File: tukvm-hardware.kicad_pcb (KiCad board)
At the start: 2 copper layers, 90.5 x 68.9 mm, 97 parts, among them J1 PCIexpress_x1, J2 PCIexpress_bracket, J3 HDMI_A, J4 USB_C_Receptacle_USB2.0, J5 Conn_02x08_Odd_Even, J6 USB_9P, J7 Conn_01x04, U1 M24C64-RMN6TP, U10 TLP172GM, U11 CH340N, U2 MS2109, U3 MCORE-H616, U4 DP1435-5V, U5 TLP172GM, U6 TLP172GM, U7 MT3520B, U8 MT3520B, U9 TLP172GM, Y1 24MHz 12pF

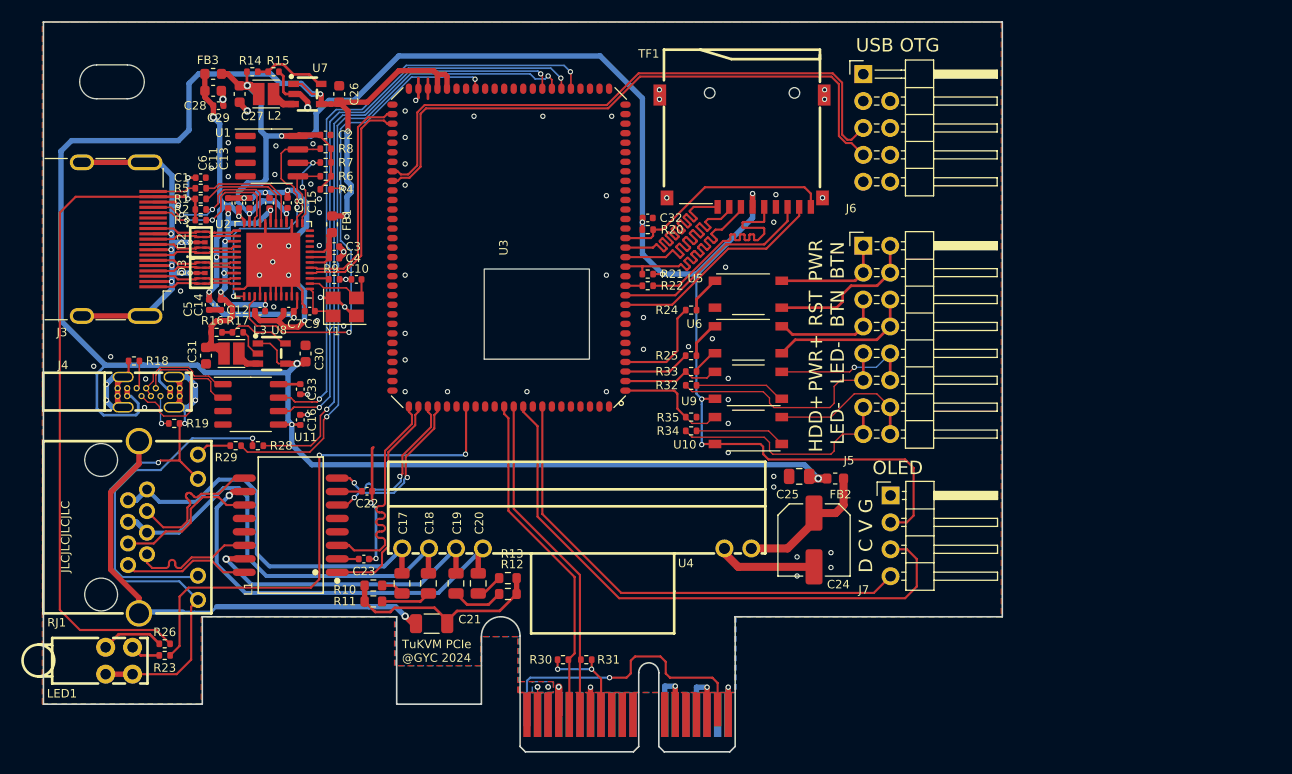
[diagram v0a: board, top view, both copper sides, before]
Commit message: Update pcb & sch for T113 SOM
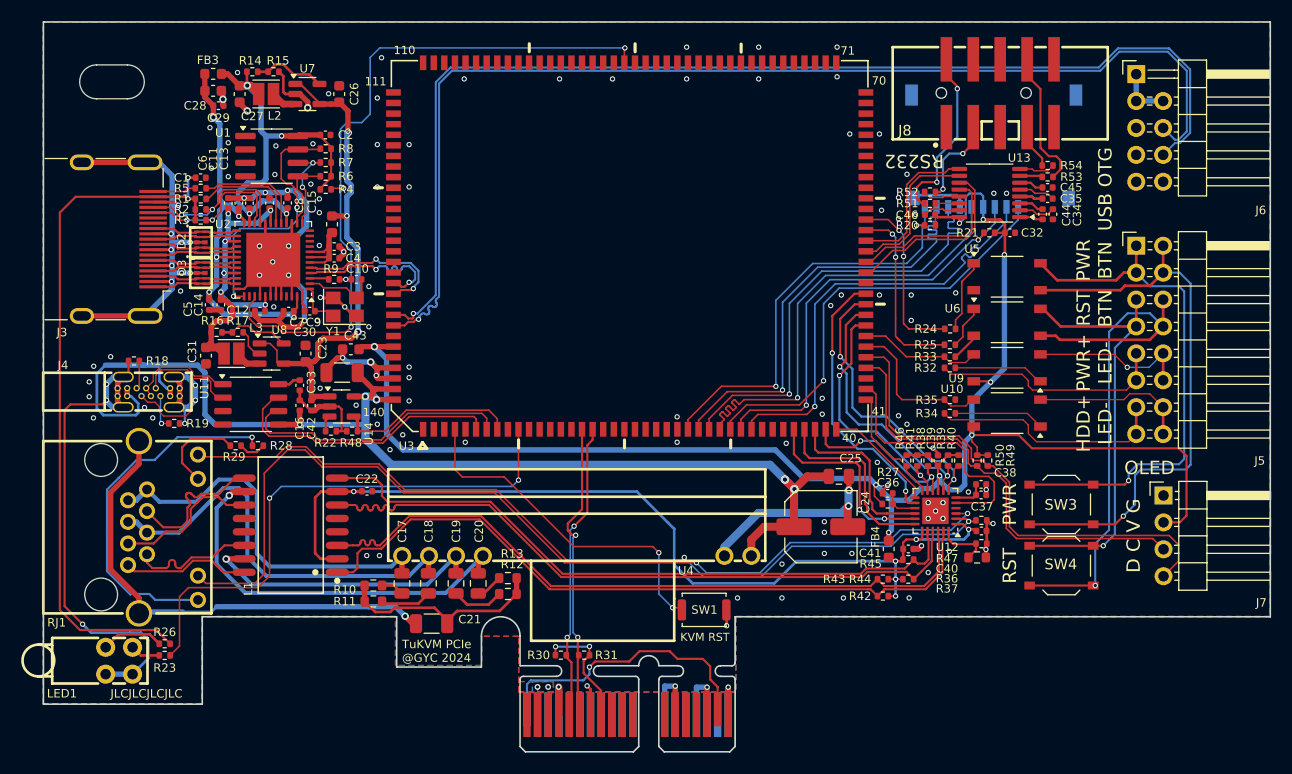
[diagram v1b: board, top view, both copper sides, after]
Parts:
- removed FB2: 600Ω@100MHz, Inductor_SMD:L_0603_1608Metric
- added C34: 100nF, Capacitor_SMD:C_0402_1005Metric, F.Cu at (158.8, 143.4)
- added C35: 100nF, Capacitor_SMD:C_0402_1005Metric, F.Cu at (159.3, 141.9)
- added C36: 100nF, Capacitor_SMD:C_0402_1005Metric, F.Cu at (144.2, 169.7)
- added C37: 100nF, Capacitor_SMD:C_0402_1005Metric, F.Cu at (153.0, 169.9)
- added C38: 1uF, Capacitor_SMD:C_0402_1005Metric, F.Cu at (153.0, 168.9)
- added C39: 100nF, Capacitor_SMD:C_0402_1005Metric, F.Cu at (148.9, 166.6)
- added C40: 100nF, Capacitor_SMD:C_0402_1005Metric, F.Cu at (153.0, 173.3)
- added C41: 100nF, Capacitor_SMD:C_0402_1005Metric, F.Cu at (146.1, 175.0)
- added C42: 1uF, Capacitor_SMD:C_0402_1005Metric, F.Cu at (89.8, 161.4)
- added C43: 10uF, Capacitor_SMD:C_0603_1608Metric, F.Cu at (93.5, 156.1)
- added C44: 100nF, Capacitor_SMD:C_0402_1005Metric, F.Cu at (159.8, 143.4)
- added C45: 100nF, Capacitor_SMD:C_0402_1005Metric, F.Cu at (159.3, 140.8)
- added C46: 100nF, Capacitor_SMD:C_0402_1005Metric, F.Cu at (148.2, 143.4)
- added FB4: 600Ω@100MHz, Inductor_SMD:L_0603_1608Metric, F.Cu at (144.3, 175.0)
- added J8: RS232_MALE, easyeda2kicad:IDC-SMD_10P-P2.54-V-R2-C5-S9.50, F.Cu at (154.8, 131.9)
- added R27: 5.1kΩ, Resistor_SMD:R_0402_1005Metric, F.Cu at (144.2, 170.7)
- added R36: 22kΩ, Resistor_SMD:R_0402_1005Metric, F.Cu at (153.0, 174.5)
- added R37: 27kΩ, Resistor_SMD:R_0603_1608Metric, F.Cu at (152.6, 175.8)
- added R38: 5.1kΩ, Resistor_SMD:R_0402_1005Metric, F.Cu at (148.0, 166.6)
- added R39: 5.1kΩ, Resistor_SMD:R_0402_1005Metric, F.Cu at (149.9, 166.6)
- added R40: 5.1kΩ, Resistor_SMD:R_0402_1005Metric, F.Cu at (150.9, 166.6)
- added R41: 5.1kΩ, Resistor_SMD:R_0402_1005Metric, F.Cu at (147.0, 166.6)
- added R42: 49.9Ω, Resistor_SMD:R_0402_1005Metric, F.Cu at (143.7, 179.4)
- added R43: 49.9Ω, Resistor_SMD:R_0402_1005Metric, F.Cu at (143.7, 177.8)
- added R44: 49.9Ω, Resistor_SMD:R_0402_1005Metric, F.Cu at (146.1, 177.8)
- added R45: 49.9Ω, Resistor_SMD:R_0402_1005Metric, F.Cu at (146.1, 176.0)
- added R46: 1.5kΩ, Resistor_SMD:R_0402_1005Metric, F.Cu at (146.0, 166.6)
- added R47: 10kΩ, Resistor_SMD:R_0402_1005Metric, F.Cu at (153.0, 172.3)
- added R48: 5.1kΩ, Resistor_SMD:R_0402_1005Metric, F.Cu at (93.6, 163.9)
- added R49: 5.1kΩ, Resistor_SMD:R_0402_1005Metric, F.Cu at (153.6, 166.6)
- added R50: 5.1kΩ, Resistor_SMD:R_0402_1005Metric, F.Cu at (152.6, 166.6)
- added R51: 0Ω, Resistor_SMD:R_0402_1005Metric, F.Cu at (148.2, 142.3)
- added R52: 0Ω, Resistor_SMD:R_0402_1005Metric, F.Cu at (148.2, 141.3)
- added R53: 0Ω, Resistor_SMD:R_0402_1005Metric, F.Cu at (159.3, 139.8)
- added R54: 0Ω, Resistor_SMD:R_0402_1005Metric, F.Cu at (159.3, 138.8)
- added SW1: SKRK, Button_Switch_SMD:SW_Push_SPST_NO_Alps_SKRK, F.Cu at (126.8, 180.7)
- added SW3: TS-1187A, Button_Switch_SMD:SW_Push_1P1T_XKB_TS-1187A, F.Cu at (160.6, 170.8)
- added SW4: TS-1187A, Button_Switch_SMD:SW_Push_1P1T_XKB_TS-1187A, F.Cu at (160.6, 176.6)
- added U12: LAN8720A, Package_DFN_QFN:VQFN-24-1EP_4x4mm_P0.5mm_EP2.5x2.5mm, F.Cu at (148.7, 171.4)
- added U13: SP3232EEY, Package_SO:TSSOP-16_4.4x5mm_P0.65mm, F.Cu at (153.8, 141.4)
- added U14: SY6280AAC, Package_TO_SOT_SMD:SOT-23-5, F.Cu at (92.6, 161.5)
- C22: value 100nF -> 22pF
- C23: value 100nF -> 100uF 6.3V; footprint Capacitor_SMD:C_0402_1005Metric -> Capacitor_SMD:C_1206_3216Metric
- R14: value 680kΩ -> 100kΩ
- R15, R16, R17: value 150kΩ -> 22kΩ
- R22: value 33Ω -> 22kΩ
- TF1: moved to B.Cu
- U3: value MCORE-H616 -> TLT113-SOM; footprint tukvm:MCORE-H616 -> tukvm:SMD_140P_35X45_SOM_TLT113_PackageLength
- U7, U8: footprint easyeda2kicad:SOT-23-5_L3.0-W1.7-P0.95-LS2.8-BR -> Package_TO_SOT_SMD:SOT-23-5
- moved C32 34.2 mm to (155.7, 145.1)
- moved R22 32.9 mm to (91.6, 163.9), turned to 0 degrees
- moved R21 32.5 mm to (153.8, 145.1)
- moved R20 26.7 mm to (148.2, 144.4), turned to 0 degrees
- moved J7 25.8 mm to (170.2, 169.9)
- moved J5 25.8 mm to (167.6, 146.3)
- moved J6 25.8 mm to (167.6, 135.2)
- moved R24 24.5 mm to (150.1, 154.2)
- moved R32 24.5 mm to (150.1, 157.9)
- moved R34 24.5 mm to (150.1, 162.2)
- moved R35 24.5 mm to (150.1, 160.9)
- moved U10 24.5 mm to (155.5, 162.1)
- moved U5 24.5 mm to (155.5, 149.3)
- moved U6 24.5 mm to (155.5, 153.6)
- moved U9 24.5 mm to (155.5, 157.9)
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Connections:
- net +1V2 renamed MS_1V2
- net +3.3VA renamed MS_3V3A
- C13 pad 2: +3.3V -> MS_3V3
- C15 pad 2: +3.3V -> MS_3V3
- C2 pad 2: +3.3V -> MS_3V3
- C22 pad 1: Earth -> PHY_VDDA
- C22 pad 2: Net-(L1-RCT) -> Earth
- C23 pad 1: Earth -> +5V
- C23 pad 2: Net-(L1-TCT) -> Earth
- C24 pad 1: Net-(U4-+5V) -> +5V
- C26 pad 2: +5V -> MS_5V
- C27 pad 2: +3.3V -> MS_3V3
- C30 pad 2: +5V -> MS_5V
- FB1 pad 2: +5V -> MS_5V
- FB3 pad 1: +3.3V -> MS_3V3
- J6 pad 5: /OTG_D- -> unconnected-(J6-Pin_5-Pad5)
- J6 pad 6: unconnected-(J6-Pin_6-Pad6) -> /OTG_D-
- J6 pad 7: /OTG_D+ -> unconnected-(J6-Pin_7-Pad7)
- J6 pad 8: unconnected-(J6-Pin_8-Pad8) -> /OTG_D+
- L1 pad 1: /PHY_RD+ -> /ETH PoE/PHY_RD+
- L1 pad 2: Net-(L1-TCT) -> PHY_VDDA
- L1 pad 3: /PHY_RD- -> /ETH PoE/PHY_RD-
- L1 pad 6: /PHY_TD+ -> /ETH PoE/PHY_TD+
- L1 pad 7: Net-(L1-RCT) -> PHY_VDDA
- L1 pad 8: /PHY_TD- -> /ETH PoE/PHY_TD-
- L2 pad 2: +3.3V -> MS_3V3
- R14 pad 1: +3.3V -> MS_3V3
- R22 pad 1: /TF_CLK -> Net-(U14-ISET)
- R22 pad 2: Net-(U3-PF2/SDC0_CLK/UART0_TX/PF_EINT2) -> Earth
- R28 pad 1: Net-(RJ1-R+) -> Net-(RJ1-R-)
- R28 pad 2: /PHY_ACT -> Earth
- R29 pad 1: Net-(RJ1-L+) -> Net-(RJ1-L-)
- R29 pad 2: /PHY_SPD -> Earth
- R4 pad 2: +3.3V -> MS_3V3
- R6 pad 1: +3.3V -> MS_3V3
- R7 pad 1: +3.3V -> MS_3V3
- R8 pad 1: +3.3V -> MS_3V3
- RJ1 pad 10: Earth -> Net-(RJ1-L-)
- RJ1 pad 11: Net-(RJ1-R+) -> /ETH PoE/LED1
- RJ1 pad 12: Earth -> Net-(RJ1-R-)
- RJ1 pad 9: Net-(RJ1-L+) -> /ETH PoE/LED2
- U1 pad 8: +3.3V -> MS_3V3
- U2 pad 16: +3.3V -> MS_3V3
- U2 pad 23: +3.3V -> MS_3V3
- U3 pad 1: /HDD_LED -> unconnected-(U3A-REFCLK_OUT-Pad1)
- U3 pad 10: /TF_D1 -> /HEART_BEAT_LED
- U3 pad 11: /TF_D0 -> unconnected-(U3A-PG2/SDC1_D0/UART3_RTS/RGMII_RXD1/RMII_RXD1/UART4_TX/PG_EINT2-Pad11)
- U3 pad 12: Net-(U3-PF2/SDC0_CLK/UART0_TX/PF_EINT2) -> unconnected-(U3A-PG1/SDC1_CMD/UART3_RX/RGMII_RXD0/RMII_RXD0/PWM6/PG_EINT1-Pad12)
- U3 pad 13: Earth -> unconnected-(U3A-PG0/SDC1_CLK/UART3_TX/RGMII_RXCTRL/RMII_CRS_DV/PWM7/PG_EINT0-Pad13)
- U3 pad 14: /TF_CMD -> unconnected-(U3A-PG10/PWM3/TWI3_SCK/RGMII_RXCK/CLK_FANOUT0/IR_RX/PG_EINT10-Pad14)
- U3 pad 15: /TF_D3 -> unconnected-(U3A-PG12/I2S1_LRCK/TWI0_SCK/RGMII_TXCTRL/RMII_TXEN/CLK_FANOUT2/PWM0/UART1_TX/PG_EINT12-Pad15)
- U3 pad 16: /TF_D2 -> /SMDAT
- U3 pad 17: /TF_DET -> /SMCLK
- U3 pad 2: /PWR_LED -> unconnected-(U3A-FEL-Pad2)
- U3 pad 25: unconnected-(U3-PI7/RGMII_TXD3/RMII_NULL/UART2_RTS/TS0_SYNC/TWI1_SCK/PI_EINT7-Pad25) -> Earth
- U3 pad 26: unconnected-(U3-PI8/RGMII_TXD2/RMII_NULL/UART2_CTS/TS0_DVLD/TWI1_SDA/PI_EINT8-Pad26) -> /TF_DET
- U3 pad 27: unconnected-(U3-PI9/RGMII_TXD1/RMII_TXD1/UART3_TX/TS0_D0/TWI2_SCK/PI_EINT9-Pad27) -> /TF_D1
- U3 pad 28: unconnected-(U3-PI10/RGMII_TXD0/RMII_TXD0/UART3_RX/TS0_D1/TWI2_SDA/PI_EINT10-Pad28) -> /TF_D0
- U3 pad 29: unconnected-(U3-PI11/RGMII_TXCK/RMII_TXCK/UART3_RTS/TS0_D2/PWM1/PI_EINT11-Pad29) -> /TF_CLK
- U3 pad 3: /ATX_RST -> unconnected-(U3A-NMI-Pad3)
- U3 pad 30: unconnected-(U3-PI12/RGMII_TXCTL/RMII_TXEN/UART3_CTS/TS0_D3/PWM2/PI_EINT12-Pad30) -> /TF_D2
- U3 pad 31: Earth -> /TF_CMD
- U3 pad 32: unconnected-(U3-PI13/RGMII_CLKIN/RMII_NULL/UART4_TX/TS0_D4/PWM3/PI_EINT13-Pad32) -> /TF_D3
- U3 pad 33: unconnected-(U3-PI14/MDC/UART4_RX/TS0_D5/PWM4/PI_EINT14-Pad33) -> Earth
- U3 pad 36: /U0TXD -> /RMII_TXD0
- U3 pad 37: /U0RXD -> /RMII_TXD1
- U3 pad 38: /PHY_SPD -> /RMII_TXEN
- U3 pad 39: /PHY_ACT -> /RMII_RXER
- U3 pad 4: /ATX_PWR -> Net-(U3A-RESET)
- U3 pad 40: unconnected-(U3-PH4/SPDIF_OUT/TWI3_SCK/PH_EINT4-Pad40) -> /RMII_MDC
- U3 pad 41: unconnected-(U3-PH5/UART2_TX/H_I2S3_MCLK/SPI1_CS0/TWI3_SDA/PH_EINT5-Pad41) -> /RMII_MDIO
- U3 pad 42: unconnected-(U3-PH6/UART2_RX/H_I2S3_BCLK/SPI1_CLK/TWI4_SCK/PH_EINT6-Pad42) -> /RMII_CLK25M
- U3 pad 44: unconnected-(U3-PH8/UART2_CTS/H_I2S3_DOUT0/SPI1_MISO/H_I2S3_DIN1/PH_EINT8-Pad44) -> /OLED_SCL
- U3 pad 45: unconnected-(U3-PH9/H_I2S3_DIN0/SPI1_CS1/H_I2S3_DOUT1/PH_EINT9-Pad45) -> /OLED_SDA
- U3 pad 46: /MS_STATUS -> /HDD_LED
- U3 pad 47: unconnected-(U3-PWRON-Pad47) -> /PWR_LED
- U3 pad 48: unconnected-(U3-VCC3V3-Pad48) -> /RMII_CRS_DV
- U3 pad 49: +5V -> /RMII_RXD0
- U3 pad 5: unconnected-(U3-PG10/H_I2S2_MCLK/X32KFOUT/AC_MCLK/PG_EINT10-Pad5) -> Earth
- U3 pad 50: +5V -> /RMII_RXD1
- U3 pad 51: Earth -> /RMII_REFCLK
- U3 pad 53: unconnected-(U3-RESET-Pad53) -> /M232_RXD
- U3 pad 54: Earth -> /M232_TXD
- U3 pad 55: /MS_USBD- -> /M232_CTS
- U3 pad 56: /MS_USBD+ -> /M232_RTS
- U3 pad 57: Earth -> /ATX_RST
- U3 pad 58: unconnected-(U3-USB2_DM-Pad58) -> /ATX_PWR
- U3 pad 6: unconnected-(U3-PC0/SPI0_CLK/PC_EINT0-Pad6) -> /U0TXD
- U3 pad 60: Earth -> unconnected-(U3B-PB4/LCD0_D8/I2S2_DOUT0/TWI1_SCK/I2S2_DIN1/LCD0_D20/UART5_TX/CAN1_TX0/PB_EINT4-Pad60)
- U3 pad 61: /OTG_D- -> unconnected-(U3B-PB5/LCD0_D9/I2S2_BCLK/TWI1_SDA/PWM0/LCD0_D21/UART5_RX/CAN1_RX0/PB_EINT5-Pad61)
- U3 pad 62: /OTG_D+ -> unconnected-(U3B-PB6/LCD0_D16/I2S2_LRCK/TWI3_SCK/PWM1/LCD0_D22/UART3_TX/CPUBIST0/PB_EINT6-Pad62)
- U3 pad 63: Earth -> unconnected-(U3B-PB7/LCD0_D17/I2S2_MCLK/TWI3_SDA/IR_RX/LCD0_D23/UART3_RX/CPUBIST1/PB_EINT7-Pad63)
- U3 pad 66: unconnected-(U3-LINEOUTL-Pad66) -> Earth
- U3 pad 7: unconnected-(U3-PC2/SPI0_MOSI/PC_EINT2-Pad7) -> /U0RXD
- U3 pad 71: unconnected-(U3-HCEC-Pad71) -> Earth
- U3 pad 72: Earth -> unconnected-(U3C-PD4/LCD0_D6/LVDS0_V2P/DSI_CKP/UART2_CTS/PD_EINT4-Pad72)
- U3 pad 75: Earth -> unconnected-(U3C-PD7/LCD0_D11/LVDS0_CKN/DSI_D2N/UART4_TX/PD_EINT7-Pad75)
- U3 pad 8: unconnected-(U3-PC4/SPI0_MISO/BOOT_SEL2/PC_EINT4-Pad8) -> /MS_PWREN
- U3 pad 81: Earth -> unconnected-(U3C-PD12/LCD0_D18/LVDS1_V1P/SPI1_MOSI/DBI_SDO/TWI0_SDA/PD_EINT12-Pad81)
- U3 pad 84: Earth -> unconnected-(U3C-PD15/LCD0_D21/LVDS1_V2N/SPI1_WP/DBI_TE/IR_RX/PD_EINT15-Pad84)
- U3 pad 85: /PHY_RD- -> Earth
- U3 pad 86: /PHY_RD+ -> unconnected-(U3C-PD16/LCD0_D22/LVDS1_CKP/DMIC_DATA3/PWM0/PD_EINT16-Pad86)
- U3 pad 87: /PHY_TD- -> unconnected-(U3C-PD17/LCD0_D23/LVDS1_CKN/DMIC_DATA2/PWM1/PD_EINT17-Pad87)
- U3 pad 88: /PHY_TD+ -> unconnected-(U3C-PD18/LCD0_CLK/LVDS1_V3P/DMIC_DATA1/PWM2/PD_EINT18-Pad88)
- U3 pad 89: Earth -> unconnected-(U3C-PD19/LCD0_DE/LVDS1_V3N/DMIC_DATA0/PWM3/PD_EINT19-Pad89)
- U3 pad 91: /HEART_BEAT_LED -> /MS_STATUS
- U3 pad 92: unconnected-(U3-PG11/H_I2S2_BCLK/BIST_RESULT0/AC_SYNC/PG_EINT11-Pad92) -> Earth
- U3 pad 95: /SMCLK -> unconnected-(U3C-LINEINR-Pad95)
- U3 pad 96: /SMDAT -> unconnected-(U3C-LINEINL-Pad96)
- U3 pad 97: /OLED_SCL -> Earth
- U3 pad 99: /OLED_SDA -> unconnected-(U3C-MIC_DET-Pad99)
- U4 pad 6: Net-(U4-+5V) -> +5V
- U7 pad 1: +5V -> MS_5V
- U7 pad 4: +5V -> MS_5V
- U8 pad 1: +5V -> MS_5V
- U8 pad 4: +5V -> MS_5V
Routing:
- net /ETH PoE/LED1: track 0.00 -> 92.0 mm, vias 0 -> 2
- net PHY_VDDA: track 0.00 -> 88.8 mm, vias 0 -> 6
- net /ETH PoE/LED2: track 0.00 -> 82.9 mm, vias 0 -> 2
- net /ETH PoE/PHY_RD+: track 0.00 -> 67.9 mm
- net /ETH PoE/PHY_RD-: track 0.00 -> 66.8 mm
- net +5V: track 187.4 -> 121.4 mm, vias 6 -> 5
- net /ETH PoE/PHY_TD+: track 0.00 -> 65.3 mm
- net /ETH PoE/PHY_TD-: track 0.00 -> 63.7 mm
- net /PHY_SPD: track 62.5 -> 0.00 mm, vias 2 -> 0
- net /PHY_ACT: track 58.9 -> 0.00 mm, vias 2 -> 0
- net /OTG_D+: track 57.4 -> 108.1 mm, vias 0 -> 1
- net /OTG_D-: track 57.4 -> 108.0 mm, vias 0 -> 1
- net MS_5V: track 0.00 -> 48.6 mm, vias 0 -> 3
- net MS_3V3: track 0.00 -> 40.1 mm, vias 0 -> 4
- net /GPIO/ATX_PWR-: track 14.6 -> 54.1 mm, vias 0 -> 1
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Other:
- board size 90.5 x 68.9 mm -> 115.8 x 68.9 mm
- board text added: "KVM RST"
- board text added: "PWR"
- board text added: "RS232"
- board text added: "RST"
